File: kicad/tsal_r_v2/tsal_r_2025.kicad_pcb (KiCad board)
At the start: 2 copper layers, 78.7 x 63.5 mm, 47 parts, among them J1 Conn_01x02_Pin, J2 Conn_01x02_Pin, U1 TL431LP, U2 LTV-817, U3 B1212, U4 2N7002, U5 2N7002, U6 NCE60P04R

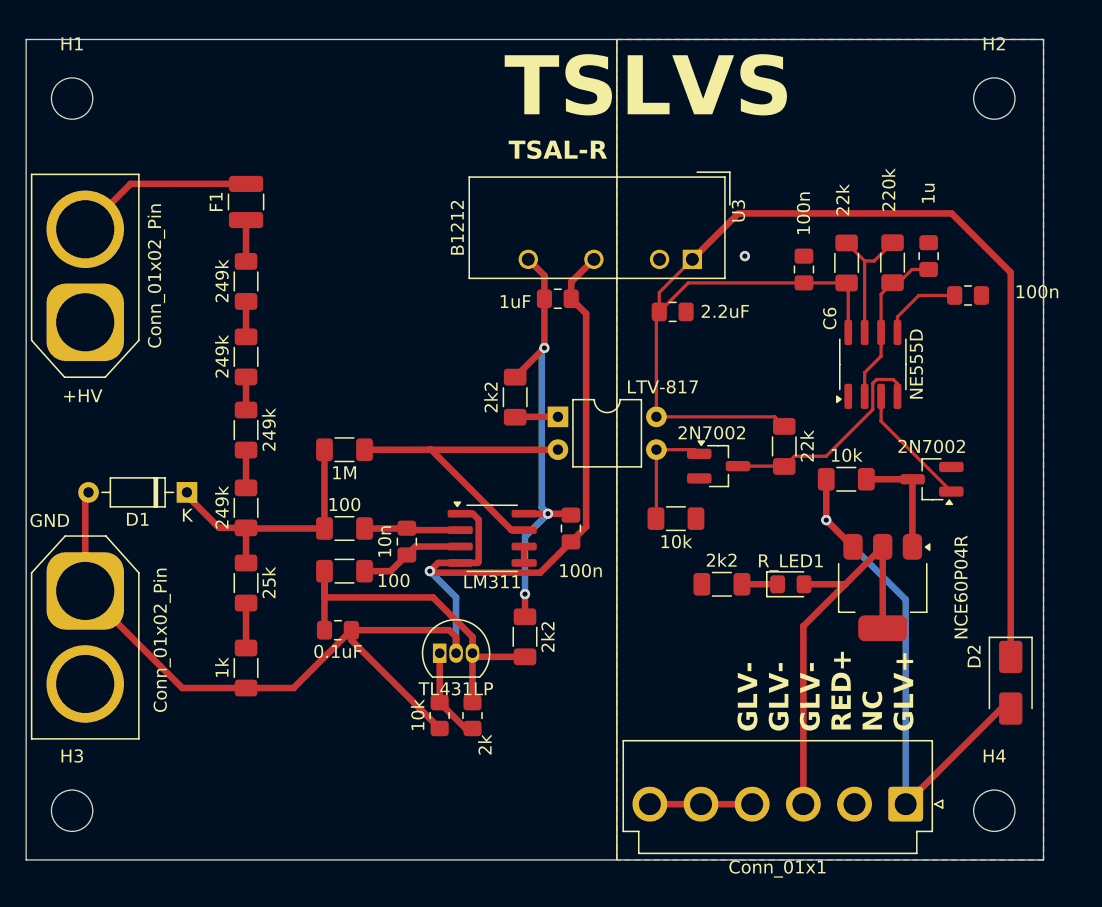
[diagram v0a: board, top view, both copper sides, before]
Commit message: TSAL-R v3.0
Redesigned the TSAL-R, currently v3. with naming RBR-TSAL-R v3.0
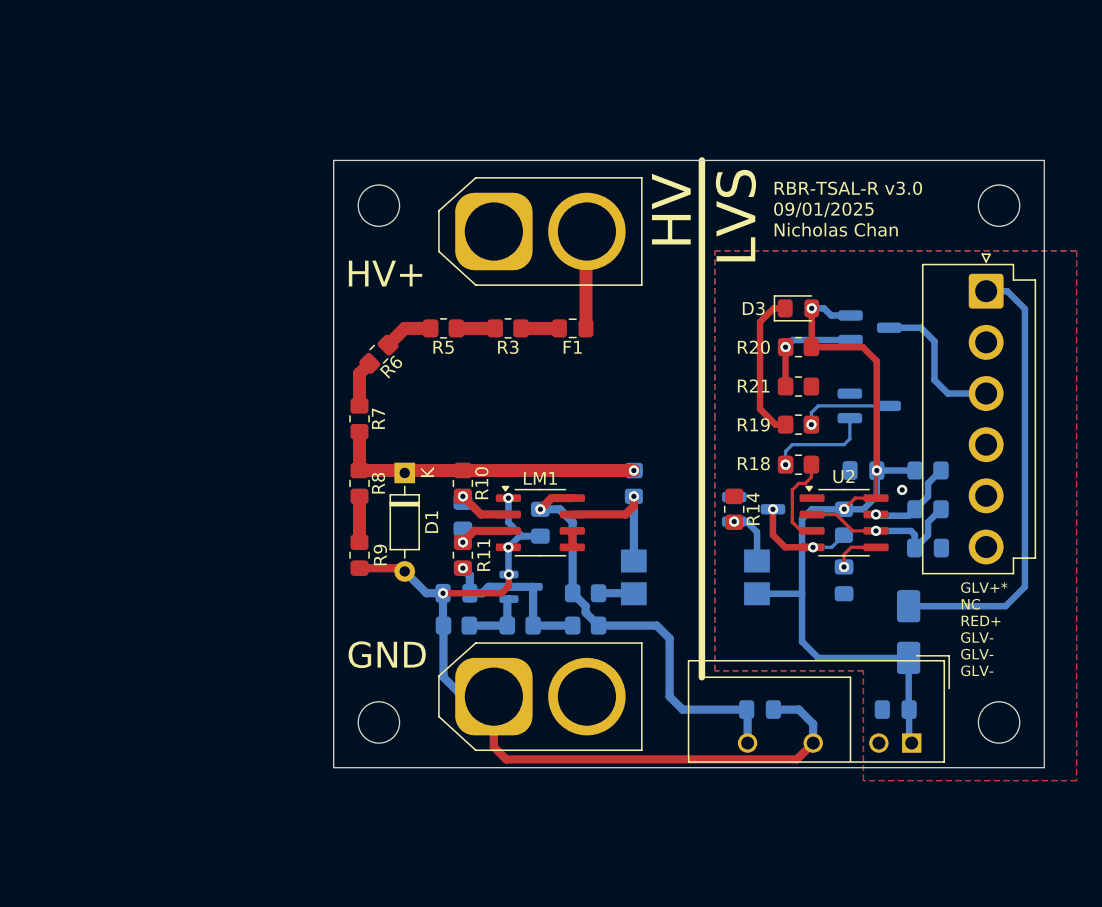
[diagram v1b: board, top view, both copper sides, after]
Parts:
- removed NE555D1: NE555D, Package_SO:SOIC-8_3.9x4.9mm_P1.27mm
- removed R_LED1: VHI, LED_SMD:LED_0805_2012Metric_Pad1.15x1.40mm_HandSolder
- removed U5: 2N7002, Package_TO_SOT_SMD:SOT-23_Handsoldering
- removed U6: NCE60P04R, Package_TO_SOT_SMD:SOT-223-3_TabPin2
- added D3: LED, LED_SMD:LED_0805_2012Metric_Pad1.15x1.40mm_HandSolder, F.Cu at (136.0, 61.5)
- added Q1: MMBT3904, Package_TO_SOT_SMD:SOT-23_Handsoldering, B.Cu at (141.4, 69.0)
- added Q3: AO3401A, Package_TO_SOT_SMD:SOT-23_Handsoldering, B.Cu at (141.5, 63.0)
- added R20: 1k, Resistor_SMD:R_0805_2012Metric_Pad1.20x1.40mm_HandSolder, F.Cu at (136.0, 64.5)
- added R21: 100k, Resistor_SMD:R_0805_2012Metric_Pad1.20x1.40mm_HandSolder, F.Cu at (136.0, 67.5)
- added U7: LTV-817S, Package_DIP:SMDIP-4_W9.53mm, B.Cu at (128.0, 82.3)
- C1, C2, C3, C4, C5, C6, C7, C8, D2, R1, R2, U4: moved to B.Cu
- F1: footprint Fuse:Fuse_1210_3225Metric -> Fuse:Fuse_0805_2012Metric_Pad1.15x1.40mm_HandSolder
- R10, R11, R14, R3, R5, R6, R7, R8, R9: footprint Resistor_SMD:R_1206_3216Metric_Pad1.30x1.75mm_HandSolder -> Resistor_SMD:R_0805_2012Metric_Pad1.20x1.40mm_HandSolder
- R12, R13, R15, R16, R17, R4: footprint Resistor_SMD:R_1206_3216Metric_Pad1.30x1.75mm_HandSolder -> Resistor_SMD:R_0805_2012Metric_Pad1.20x1.40mm_HandSolder; moved to B.Cu
- R18: value 10k -> 1k; footprint Resistor_SMD:R_1206_3216Metric_Pad1.30x1.75mm_HandSolder -> Resistor_SMD:R_0805_2012Metric_Pad1.20x1.40mm_HandSolder
- R19: value 2k2 -> 1k; footprint Resistor_SMD:R_1206_3216Metric_Pad1.30x1.75mm_HandSolder -> Resistor_SMD:R_0805_2012Metric_Pad1.20x1.40mm_HandSolder
- U1: value TL431LP -> TLV431BQDBZR; footprint Package_TO_SOT_THT:TO-92_Inline -> Package_TO_SOT_SMD:SOT-23; moved to B.Cu
- U2: value LTV-817 -> NE555D; footprint Package_DIP:DIP-4_W7.62mm -> Package_SO:SOIC-8_3.9x4.9mm_P1.27mm
- moved U3 41.1 mm to (144.7, 95.1)
- moved Conn_01x1 40.2 mm to (150.5, 60.1), turned to -90 degrees
- moved C4 35.4 mm to (133.0, 92.5)
- moved C5 35.3 mm to (143.5, 92.5), turned to 0 degrees
- moved J2 32.7 mm to (112.4, 91.5), turned to 0 degrees
- moved J1 32.4 mm to (112.4, 55.5), turned to 0 degrees
- moved F1 27.1 mm to (118.5, 63.0), turned to 0 degrees
- moved H1 25.1 mm to (103.5, 53.5)
- moved H3 24.7 mm to (103.5, 93.5)
- moved C7 24.0 mm to (139.5, 82.5), turned to 90 degrees
- moved G*** 23.7 mm to (115.5, 66.0)
- moved U2 23.6 mm to (139.5, 78.0)
- moved C8 22.6 mm to (146.0, 80.0), turned to 180 degrees
- moved R12 22.5 mm to (123.2, 75.0), turned to -90 degrees
- moved R3 20.6 mm to (113.5, 63.0), turned to 180 degrees
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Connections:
- C7 pad 2: Net-(NE555D1-CV) -> Net-(U2-CV)
- C8 pad 2: Net-(NE555D1-THR) -> Net-(U2-THR)
- R15 pad 1: Net-(NE555D1-R) -> Net-(U2-R)
- R16 pad 1: Net-(NE555D1-DIS) -> Net-(U2-DIS)
- R17 pad 1: Net-(NE555D1-THR) -> Net-(U2-THR)
- R17 pad 2: Net-(NE555D1-DIS) -> Net-(U2-DIS)
- R18 pad 1: Net-(U5-D) -> Net-(U2-Q)
- R18 pad 2: GLV+ -> Net-(Q1-B)
- R19 pad 2: GLV- -> Net-(Q1-C)
- U2 pad 1: Net-(R13-Pad2) -> GLV-
- U2 pad 2: Net-(LM1-Pad7) -> Net-(U2-THR)
- U2 pad 3: Net-(U4-G) -> Net-(U2-Q)
- U2 pad 4: VCC -> Net-(U2-R)
- U4 pad 3: Net-(NE555D1-R) -> Net-(U2-R)
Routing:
- net GND: track 104.7 -> 68.8 mm, vias 1 -> 4
- net VCC: track 100.4 -> 65.1 mm, vias 0 -> 3
- net /RED+: track 31.9 -> 11.4 mm
- net Net-(NE555D1-R): track 17.4 -> 0.00 mm
- net /Vref: track 28.6 -> 13.3 mm, vias 0 -> 1
- net Net-(LM1-Pad7): track 24.9 -> 10.8 mm, vias 0 -> 1
- net Net-(U2-THR): track 0.00 -> 13.5 mm, vias 0 -> 1
- net Net-(NE555D1-THR): track 12.9 -> 0.00 mm
- net Net-(NE555D1-DIS): track 10.4 -> 0.00 mm
- net Net-(NE555D1-Q): track 9.62 -> 0.00 mm
- net Net-(D3-K): track 2.76 -> 11.6 mm
- net Net-(U5-D): track 8.82 -> 0.00 mm
- net Net-(Q3-G): track 0.00 -> 8.30 mm, vias 0 -> 1
- net Net-(U2-R): track 0.00 -> 8.21 mm, vias 0 -> 2
- net Net-(Q1-B): track 0.00 -> 8.00 mm, vias 0 -> 1
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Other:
- board size 78.7 x 63.5 mm -> 55 x 47 mm
- board text added: "GLV+* NC RED+ GLV- GLV- GLV-"
- board text added: "HV"
- board text added: "HV+"
- board text added: "RBR-TSAL-R v3.0 09/01/2025 Nicholas Chan"
- board text removed: "+HV"
- board text removed: "GLV- GLV- GLV- RED+ NC GLV+"
- board text removed: "TS"
- board text removed: "TSAL-R"
- board text removed: "TSAL-R Red Bird Racing EVRT Nicholas"
